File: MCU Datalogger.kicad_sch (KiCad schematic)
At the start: 25 parts, among them U1 24LC1025, U2 DS1337S_, U3 24LC1025, U4 ATMEGA328P-AU, Y1 32.768 KHz, Y2 16 MHz

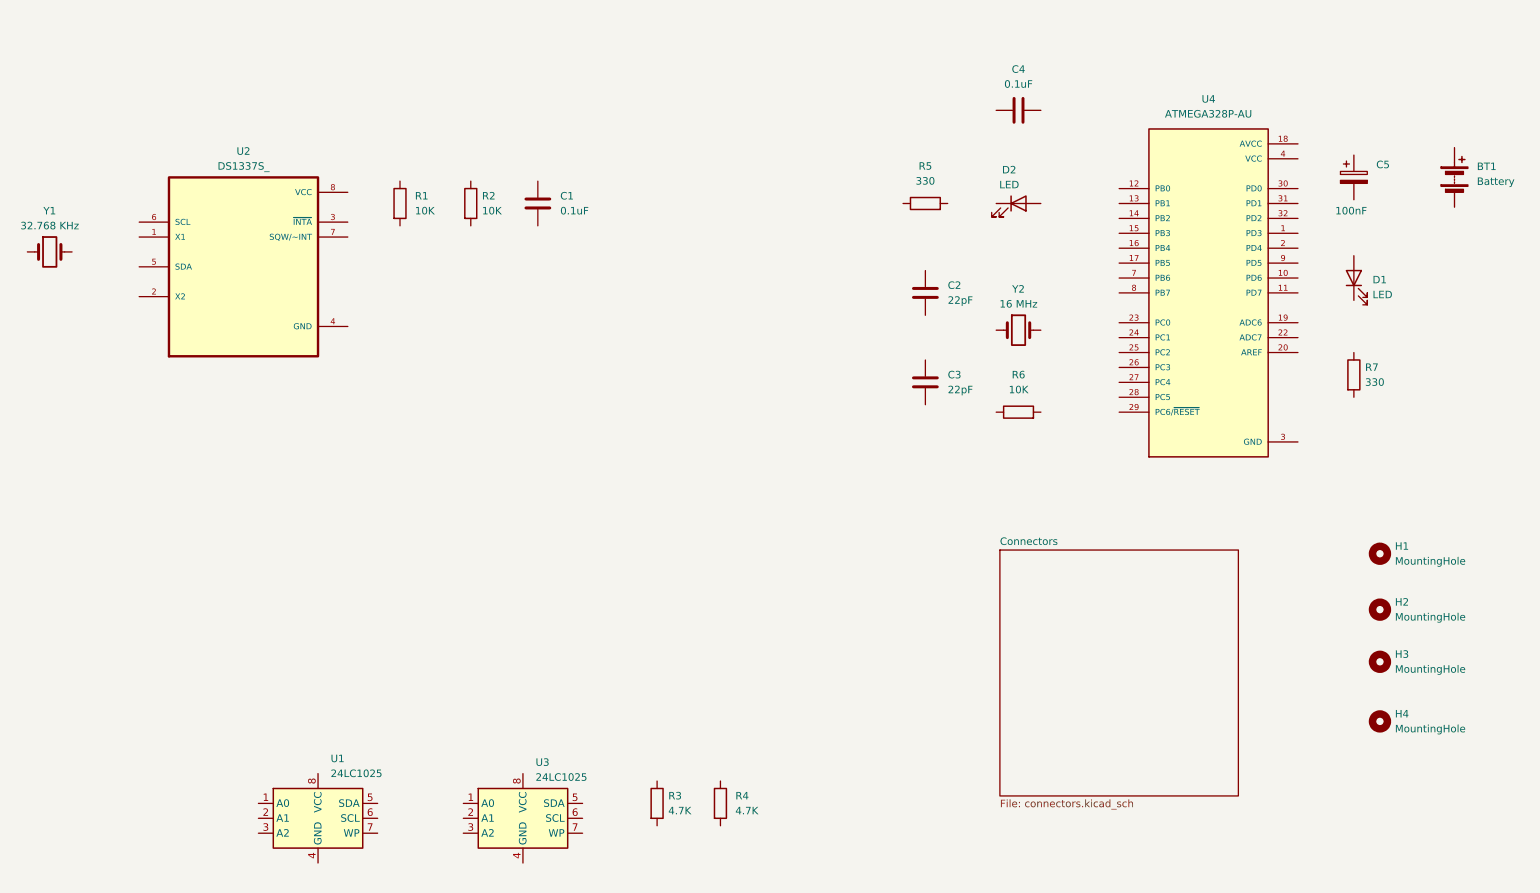
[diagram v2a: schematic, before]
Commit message: wiring on sheet 1 done
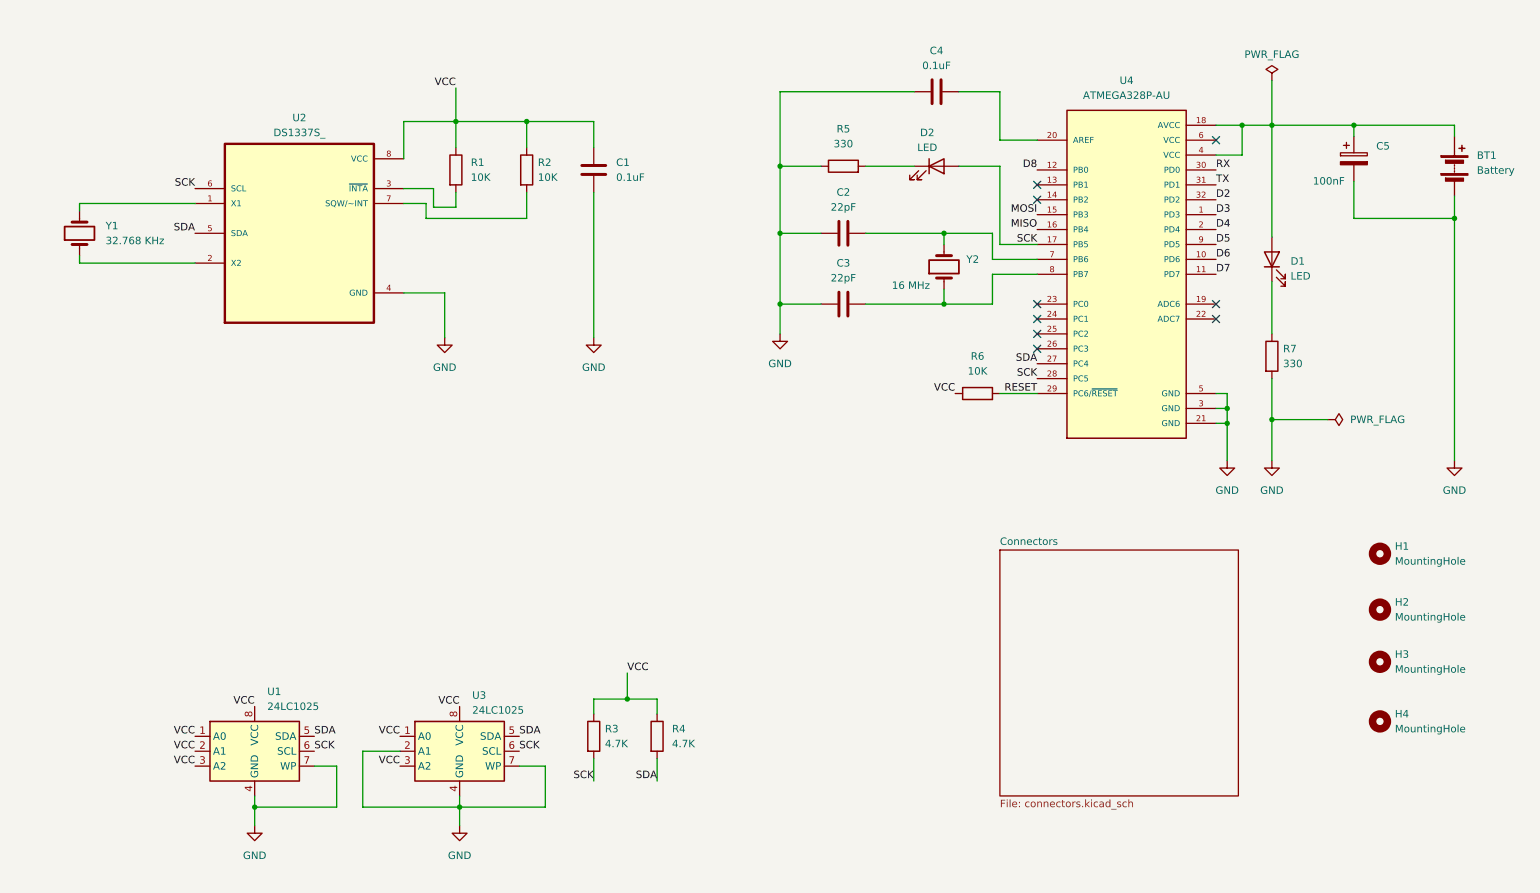
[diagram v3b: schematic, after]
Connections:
- net GND: now also BT1.2 (-), C1.2, C2.2, C3.1, C4.1, C5.2, R5.1, R7.2, U1.4 (GND), U1.7 (WP), U2.4 (GND), U3.2 (A1), U3.4 (GND), U3.7 (WP)
- net VCC: now also C1.1, R1.1, R2.1, R3.1, R4.1, R6.1, U1.1 (A0), U1.2 (A1), U1.3 (A2), U1.8 (VCC), U2.8 (VCC), U3.1 (A0), U3.3 (A2), U3.8 (VCC); no longer U4.4 (VCC), U4.6 (VCC)
- net SDA: now reaches R4.2
- net SDA: now also U1.5 (SDA), U2.5 (SDA), U3.5 (SDA), U4.27 (PC4)
- net SCK: now reaches R3.2
- net SCK: now also D2.2 (A), U1.6 (SCL), U2.6 (SCL), U3.6 (SCL), U4.17 (PB5), U4.28 (PC5)
- net at Y2.1: now also C3.2, U4.8 (PB7)
- net at Y2.2: now also C2.1, U4.7 (PB6)
- net at R1.2: now also U2.3 (~{INTA})
- net at BT1.1 (+): now also C5.1, D1.2 (A), U4.18 (AVCC), U4.4 (VCC)
- net at C4.2: now also U4.20 (AREF)
- net at D1.1 (K): now also R7.1
- net D3: now reaches U4.1 (PD3)
- net D6: now reaches U4.10 (PD6)
- net D7: now reaches U4.11 (PD7)
- net D8: now reaches U4.12 (PB0)
- net MOSI: now reaches U4.15 (PB3)
- net MISO: now reaches U4.16 (PB4)
- net D4: now reaches U4.2 (PD4)
- net RESET: now reaches U4.29 (PC6/~{RESET})
- net RESET: now also R6.2
- net RX: now reaches U4.30 (PD0)
- net TX: now reaches U4.31 (PD1)
- net D2: now reaches U4.32 (PD2)
- net D5: now reaches U4.9 (PD5)
- net at D2.1 (K): now also R5.2
- net at R2.2: now also U2.7 (SQW/~INT)
- net at Y1.1: now also U2.2 (X2)
- net at Y1.2: now also U2.1 (X1)
- no-connect marks 0 -> 9
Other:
- moved on the sheet: BT1, C1, C2, C3, C4, C5, D1, D2, R1, R2, R3, R4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

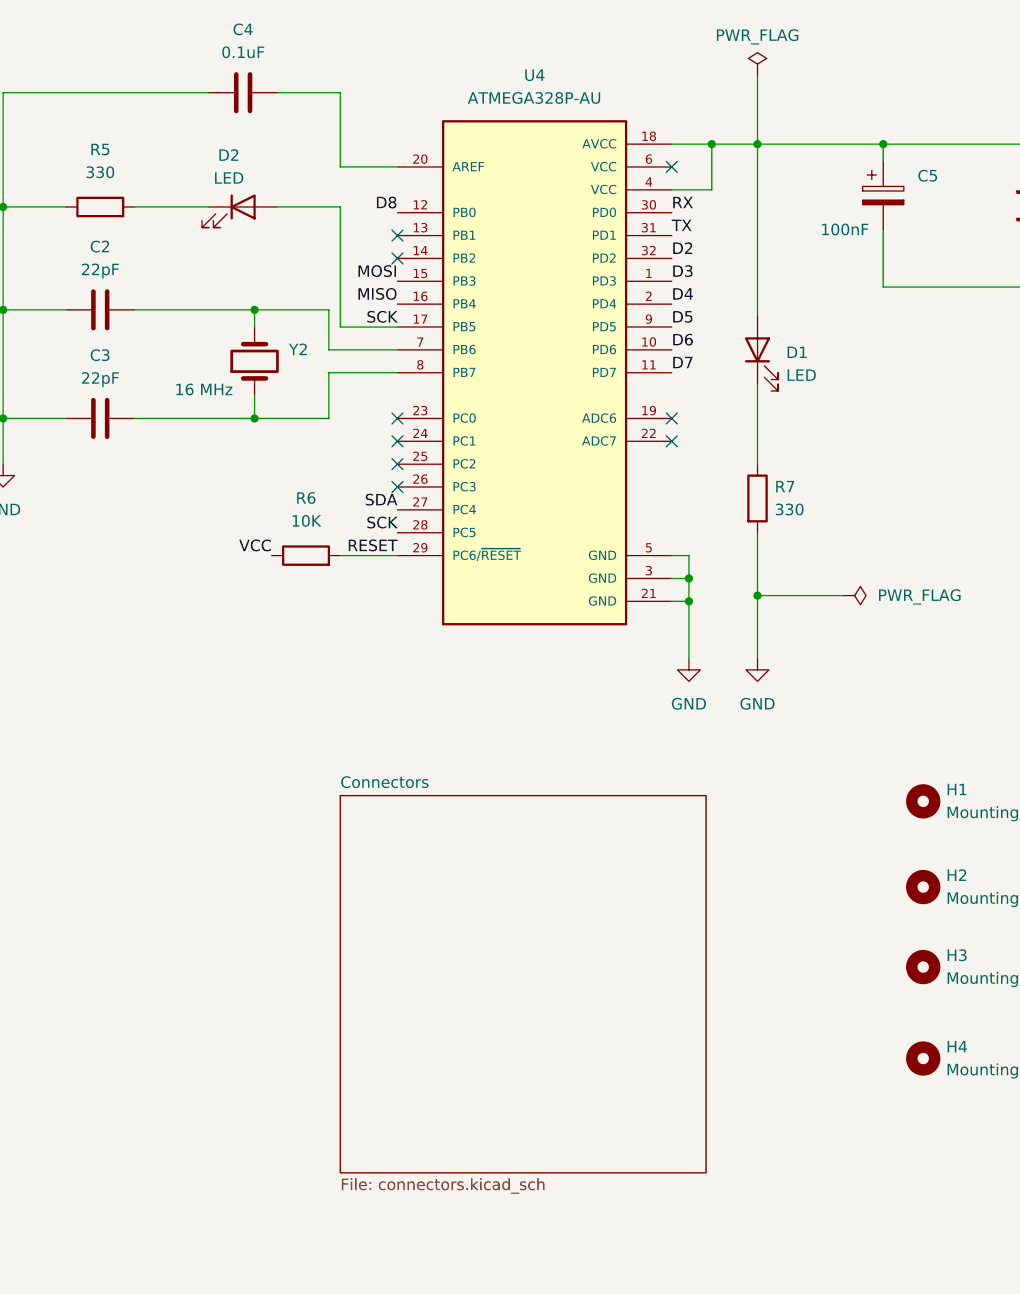
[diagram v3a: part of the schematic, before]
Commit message: wiring on sheet 2 done
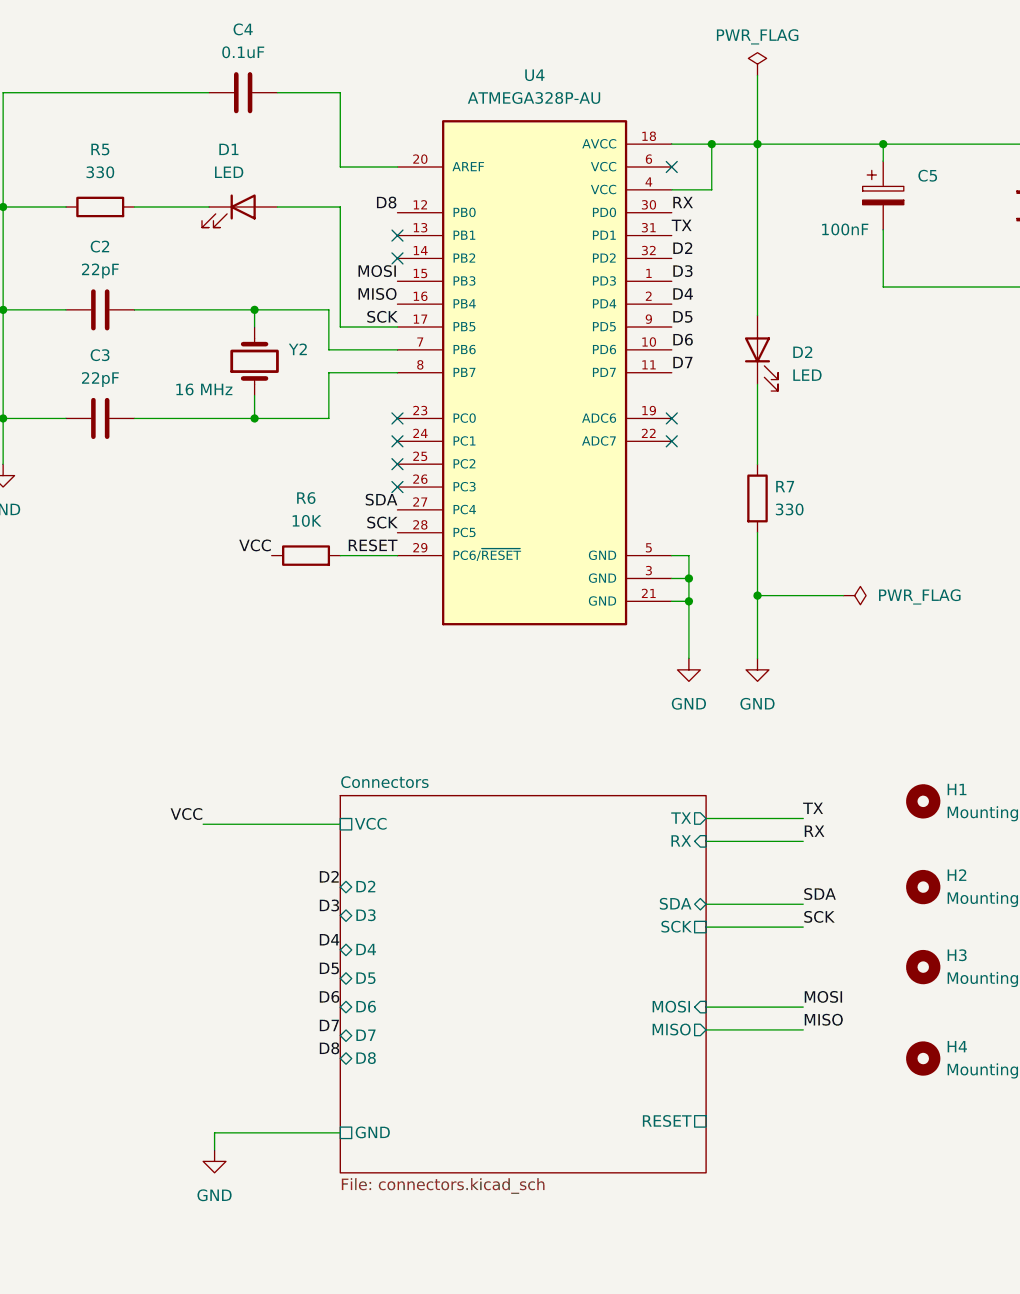
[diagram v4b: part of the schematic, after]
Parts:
- renumbered D2 to D1, D1 to D2
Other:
- sheet Connectors ports: added D2, D3, D4, D5, D6, D7, D8, GND, MISO, MOSI, RESET, RX, SCK, SDA, TX, VCC; removed none

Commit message: net
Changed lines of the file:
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@@
 	)
 	(junction
+		(at 110.49 41.91)
+		(diameter 0)
+		(color 0 0 0 0)
+	)
+	(junction
 		(at 130.175 140.335)
 		(diameter 0)
@@
 	(wire
 		(pts
-			(xy 100.965 41.91) (xy 113.03 41.91)
+			(xy 100.965 41.91) (xy 110.49 41.91)
 		)
 		(stroke
@@
 	(wire
 		(pts
+			(xy 110.49 41.91) (xy 113.03 41.91)
+		)
+		(stroke
+			(width 0)
+			(type default)
+		)
+	)
+	(wire
+		(pts
 			(xy 66.675 158.75) (xy 80.645 158.75)
 		)
@@
 		)
 	)
+	(label "RESET"
+		(at 234.315 151.13 0)
+		(effects
+			(font
+				(size 1.27 1.27)
+			)
+			(justify left bottom)
+		)
+	)
 	(label "D6"
 		(at 193.675 138.43 180)
@@
 					(unit 1)
 				)
+			)
+		)
+	)
+	(symbol
+		(lib_id "power:PWR_FLAG")
+		(at 110.49 41.91 0)
+		(unit 1)
+		(body_style 1)
+		(exclude_from_sim no)
+		(in_bom yes)
+		(on_board yes)
+		(in_pos_files yes)
+		(dnp no)
+		(fields_autoplaced yes)
+		(property "Reference" "#FLG03"
+			(at 110.49 40.005 0)
+			(hide yes)
+			(show_name no)
+			(do_not_autoplace no)
+			(effects
+				(font
+					(size 1.27 1.27)
+				)
+			)
+		)
+		(property "Value" "PWR_FLAG"
+			(at 110.49 37.465 0)
+			(show_name no)
+			(do_not_autoplace no)
+			(effects
+				(font
+					(size 1.27 1.27)
+				)
+			)
+		)
+		(property "Footprint" ""
+			(at 110.49 41.91 0)
+			(hide yes)
+			(show_name no)
+			(do_not_autoplace no)
+			(effects
+				(font
+					(size 1.27 1.27)
+				)
+			)
+		)
+		(property "Datasheet" ""
+			(at 110.49 41.91 0)
+			(hide yes)
+			(show_name no)
+			(do_not_autoplace no)
+			(effects
+				(font
+					(size 1.27 1.27)
+				)
+			)
+		)
+		(property "Description" "Special symbol for telling ERC where power comes from"
+			(at 110.49 41.91 0)
+			(hide yes)
+			(show_name no)
+			(do_not_autoplace no)
+			(effects
+				(font
+					(size 1.27 1.27)
+				)
+			)
+		)
+		(pin "1"
+		)
+		(instances
+			(project "MCU Datalogger"
+				(path "/b73ecac8-4a36-487b-b5fb-782ebc8b8ea9"
+					(reference "#FLG03")
+					(unit 1)
+				)

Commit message: completed
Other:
- note added: "EEPROM"
- note added: "MCU"
- note added: "Mounting holes"
- note added: "Real Time Clock"
- moved on the sheet: H1, H2, H3, H4
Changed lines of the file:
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@@
 		(company "Nisham Parakkal")
 	)
+	(rectangle
+		(start 48.895 130.81)
+		(end 149.86 171.45)
+		(stroke
+			(width 0)
+			(type default)
+		)
+		(fill
+			(type none)
+		)
+	)
+	(rectangle
+		(start 151.765 26.035)
+		(end 282.575 107.95)
+		(stroke
+			(width 0)
+			(type default)
+		)
+		(fill
+			(type none)
+		)
+	)
+	(rectangle
+		(start 254.635 115.57)
+		(end 280.035 157.48)
+		(stroke
+			(width 0)
+			(type default)
+		)
+		(fill
+			(type none)
+		)
+	)
+	(rectangle
+		(start 31.75 31.115)
+		(end 137.795 92.71)
+		(stroke
+			(width 0)
+			(type default)
+		)
+		(fill
+			(type none)
+		)
+	)
+	(rectangle
+		(start 173.355 111.76)
+		(end 250.825 163.195)
+		(stroke
+			(width 0)
+			(type default)
+		)
+		(fill
+			(type none)
+		)
+	)
+	(text "EEPROM"
+		(exclude_from_sim no)
+		(at 53.34 129.54 0)
+		(effects
+			(font
+				(size 1.27 1.27)
+			)
+		)
+	)
+	(text "MCU"
+		(exclude_from_sim no)
+		(at 154.305 24.765 0)
+		(effects
+			(font
+				(size 1.27 1.27)
+			)
+		)
+	)
+	(text "Real Time Clock"
+		(exclude_from_sim no)
+		(at 40.005 29.845 0)
+		(effects
+			(font
+				(size 1.27 1.27)
+			)
+		)
+	)
+	(text "Mounting holes"
+		(exclude_from_sim no)
+		(at 262.255 114.3 0)
+		(effects
+			(font
+				(size 1.27 1.27)
+			)
+		)
+	)
 	(junction
 		(at 234.95 42.545)
@@
 	(symbol
 		(lib_id "Mechanical:MountingHole")
-		(at 258.445 125.095 0)
+		(at 259.08 130.175 0)
 		(unit 1)
 		(body_style 1)
@@
 		(fields_autoplaced yes)
 		(property "Reference" "H2"
-			(at 260.985 123.8249 0)
+			(at 261.62 128.9049 0)
 			(show_name no)
 			(do_not_autoplace no)
@@
 		)
 		(property "Value" "MountingHole"
-			(at 260.985 126.3649 0)
+			(at 261.62 131.4449 0)
 			(show_name no)
 			(do_not_autoplace no)
@@
 		)
 		(property "Footprint" "MountingHole:MountingHole_2.1mm"
-			(at 258.445 125.095 0)
+			(at 259.08 130.175 0)
 			(hide yes)
 			(show_name no)
@@
 		)
 		(property "Datasheet" ""
-			(at 258.445 125.095 0)
+			(at 259.08 130.175 0)
 			(hide yes)
 			(show_name no)
@@
 		)
 		(property "Description" "Mounting Hole without connection"
-			(at 258.445 125.095 0)
+			(at 259.08 130.175 0)
 			(hide yes)
 			(show_name no)
@@
 	(symbol
 		(lib_id "Mechanical:MountingHole")
-		(at 258.445 133.985 0)
+		(at 259.08 139.065 0)
 		(unit 1)
 		(body_style 1)
@@
 		(fields_autoplaced yes)
 		(property "Reference" "H3"
-			(at 260.985 132.7149 0)
+			(at 261.62 137.7949 0)
 			(show_name no)
 			(do_not_autoplace no)
@@
 		)
 		(property "Value" "MountingHole"
-			(at 260.985 135.2549 0)
+			(at 261.62 140.3349 0)
 			(show_name no)
 			(do_not_autoplace no)
@@
 		)
 		(property "Footprint" "MountingHole:MountingHole_2.1mm"
-			(at 258.445 133.985 0)
+			(at 259.08 139.065 0)
 			(hide yes)
 			(show_name no)
@@
 		)
 		(property "Datasheet" ""
-			(at 258.445 133.985 0)
+			(at 259.08 139.065 0)
 			(hide yes)
 			(show_name no)
@@
 		)
 		(property "Description" "Mounting Hole without connection"
-			(at 258.445 133.985 0)
+			(at 259.08 139.065 0)
 			(hide yes)
 			(show_name no)
@@
 	(symbol
 		(lib_id "Mechanical:MountingHole")
-		(at 258.445 115.57 0)
+		(at 259.08 120.65 0)
 		(unit 1)
 		(body_style 1)
@@
 		(fields_autoplaced yes)
 		(property "Reference" "H1"
-			(at 260.985 114.2999 0)
+			(at 261.62 119.3799 0)
 			(show_name no)
 			(do_not_autoplace no)
@@
 		)
 		(property "Value" "MountingHole"
-			(at 260.985 116.8399 0)
+			(at 261.62 121.9199 0)
 			(show_name no)
 			(do_not_autoplace no)
@@
 		)
 		(property "Footprint" "MountingHole:MountingHole_2.1mm"
-			(at 258.445 115.57 0)
+			(at 259.08 120.65 0)
 			(hide yes)
 			(show_name no)
@@
 		)
 		(property "Datasheet" ""
-			(at 258.445 115.57 0)
+			(at 259.08 120.65 0)
 			(hide yes)
 			(show_name no)
@@
 		)
 		(property "Description" "Mounting Hole without connection"
-			(at 258.445 115.57 0)
+			(at 259.08 120.65 0)
 			(hide yes)
 			(show_name no)
@@
 	(symbol
 		(lib_id "Mechanical:MountingHole")
-		(at 258.445 144.145 0)
+		(at 259.08 149.225 0)
 		(unit 1)
 		(body_style 1)
@@
 		(fields_autoplaced yes)
 		(property "Reference" "H4"
-			(at 260.985 142.8749 0)
+			(at 261.62 147.9549 0)
 			(show_name no)
 			(do_not_autoplace no)
@@
 		)
 		(property "Value" "MountingHole"
-			(at 260.985 145.4149 0)
+			(at 261.62 150.4949 0)
 			(show_name no)
 			(do_not_autoplace no)
@@
 		)
 		(property "Footprint" "MountingHole:MountingHole_2.1mm"
-			(at 258.445 144.145 0)
+			(at 259.08 149.225 0)
 			(hide yes)
 			(show_name no)
@@
 		)
 		(property "Datasheet" ""
-			(at 258.445 144.145 0)
+			(at 259.08 149.225 0)
 			(hide yes)
 			(show_name no)
@@
 		)
 		(property "Description" "Mounting Hole without connection"
-			(at 258.445 144.145 0)
+			(at 259.08 149.225 0)
 			(hide yes)
 			(show_name no)

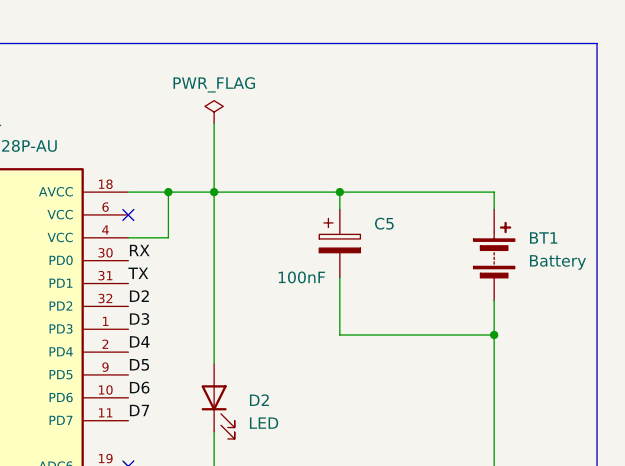
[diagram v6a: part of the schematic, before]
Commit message: finished silkscreen
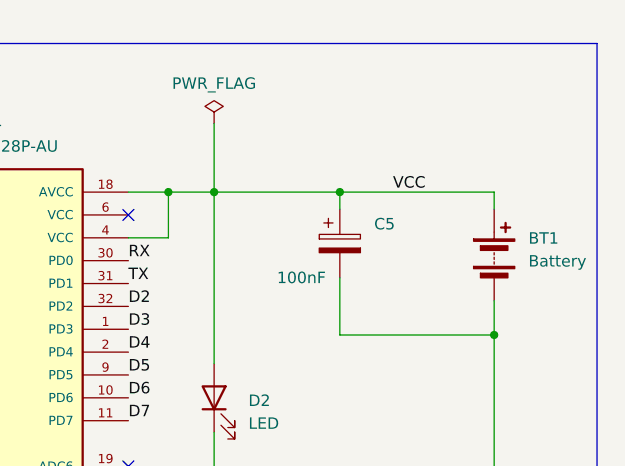
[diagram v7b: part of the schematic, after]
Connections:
- net VCC: now also BT1.1 (+), C5.1, D2.2 (A), U4.18 (AVCC), U4.4 (VCC)
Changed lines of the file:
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@@
+		)
+	)
+	(label "VCC"
+		(at 263.525 42.545 180)
+		(effects
+			(font
+				(size 1.27 1.27)
+			)
+			(justify right bottom)
 		)
 	)
